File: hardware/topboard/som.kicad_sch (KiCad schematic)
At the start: 8 parts

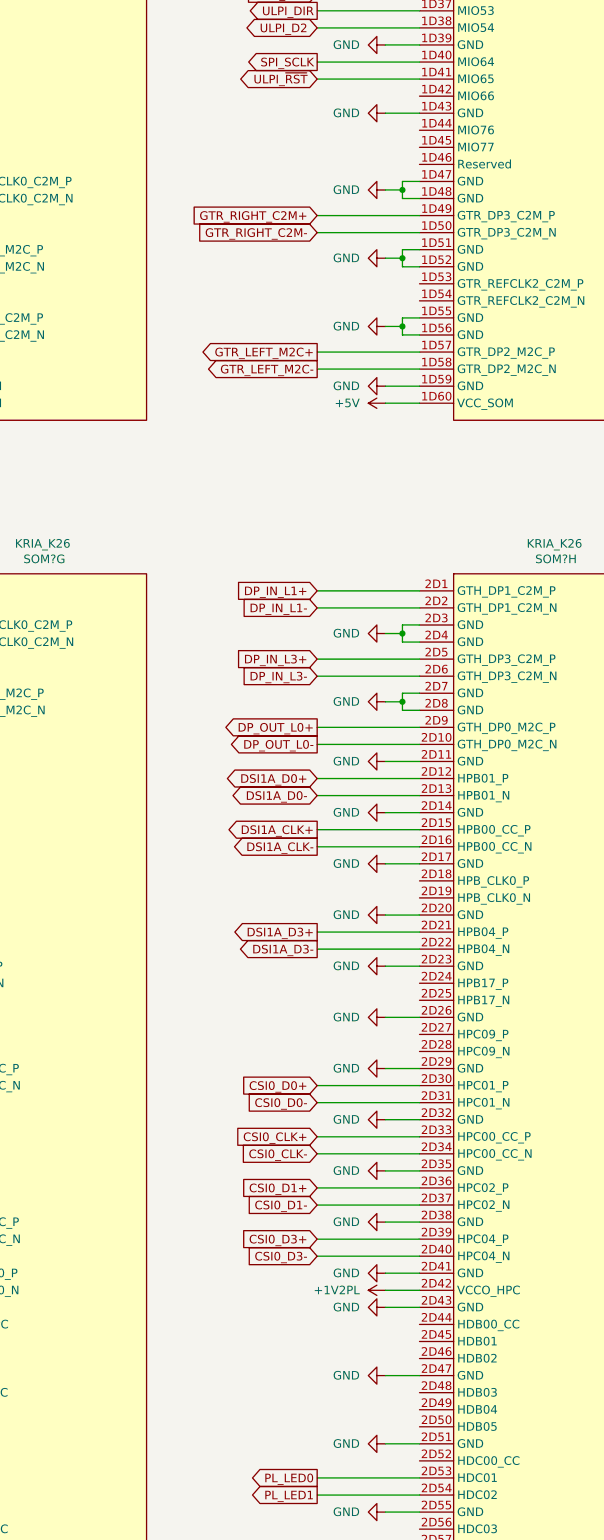
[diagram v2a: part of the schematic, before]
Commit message: Add PCIe and camera to front board
Signed-off-by: gatecat <gatecat@ds0.me>
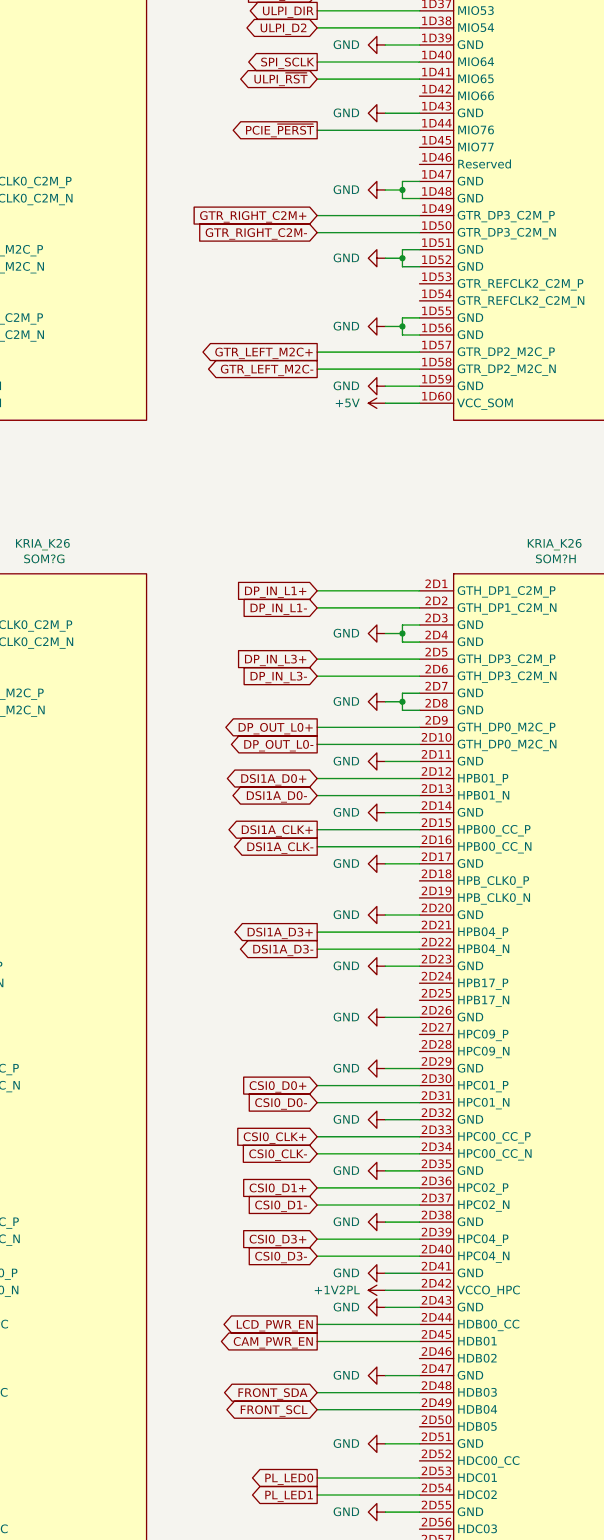
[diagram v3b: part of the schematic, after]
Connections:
- net PCIE_~{PERST}: now reaches SOM?.1D44 (MIO76)
- net LCD_PWR_EN: now reaches SOM?.2D44 (HDB00_CC)
- net CAM_PWR_EN: now reaches SOM?.2D45 (HDB01)
- net FRONT_SDA: now reaches SOM?.2D48 (HDB03)
- net FRONT_SCL: now reaches SOM?.2D49 (HDB04)
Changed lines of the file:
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@@
+    (stroke (width 0) (type default) (color 0 0 0 0))
+  )
+  (wire (pts (xy 330.2 137.16) (xy 345.44 137.16))
     (stroke (width 0) (type default) (color 0 0 0 0))
   )
@@
     (stroke (width 0) (type default) (color 0 0 0 0))
   )
+  (wire (pts (xy 330.2 314.96) (xy 345.44 314.96))
+    (stroke (width 0) (type default) (color 0 0 0 0))
+  )
+  (wire (pts (xy 330.2 317.5) (xy 345.44 317.5))
+    (stroke (width 0) (type default) (color 0 0 0 0))
+  )
+  (wire (pts (xy 330.2 325.12) (xy 345.44 325.12))
+    (stroke (width 0) (type default) (color 0 0 0 0))
+  )
+  (wire (pts (xy 330.2 327.66) (xy 345.44 327.66))
+    (stroke (width 0) (type default) (color 0 0 0 0))
+  )
   (wire (pts (xy 330.2 337.82) (xy 345.44 337.82))
     (stroke (width 0) (type default) (color 0 0 0 0))
@@
     )
   )
+  (global_label "PCIE_~{PERST}" (shape output) (at 330.2 137.16 180) (fields_autoplaced)
+    (effects (font (size 1.27 1.27)) (justify right))
+    (property "Intersheet References" "${INTERSHEET_REFS}" (id 0) (at 316.6593 137.0806 0)
+      (effects (font (size 1.27 1.27)) (justify right) hide)
+    )
+  )
   (global_label "GTR_RIGHT_C2M+" (shape input) (at 330.2 149.86 180) (fields_autoplaced)
     (effects (font (size 1.27 1.27)) (justify right))
@@
       (effects (font (size 1.27 1.27)) (justify right) hide)
     )
+  )
+  (global_label "LCD_PWR_EN" (shape output) (at 330.2 314.96 180) (fields_autoplaced)
+    (effects (font (size 1.27 1.27)) (justify right))
+    (property "Intersheet References" "${INTERSHEET_REFS}" (id 0) (at 315.8126 314.8806 0)
+      (effects (font (size 1.27 1.27)) (justify right) hide)
+    )
+  )
+  (global_label "CAM_PWR_EN" (shape output) (at 330.2 317.5 180) (fields_autoplaced)
+    (effects (font (size 1.27 1.27)) (justify right))
+    (property "Intersheet References" "${INTERSHEET_REFS}" (id 0) (at 315.5707 317.4206 0)
+      (effects (font (size 1.27 1.27)) (justify right) hide)
+    )
+  )
+  (global_label "FRONT_SDA" (shape bidirectional) (at 330.2 325.12 180) (fields_autoplaced)
+    (effects (font (size 1.27 1.27)) (justify right))
+    (property "Intersheet References" "${INTERSHEET_REFS}" (id 0) (at 317.264 325.0406 0)
+      (effects (font (size 1.27 1.27)) (justify right) hide)
+    )
+  )
+  (global_label "FRONT_SCL" (shape bidirectional) (at 330.2 327.66 180) (fields_autoplaced)
+    (effects (font (size 1.27 1.27)) (justify right))
+    (property "Intersheet References" "${INTERSHEET_REFS}" (id 0) (at 317.3245 327.5806 0)
+      (effects (font (size 1.27 1.27)) (justify right) hide)
+    )

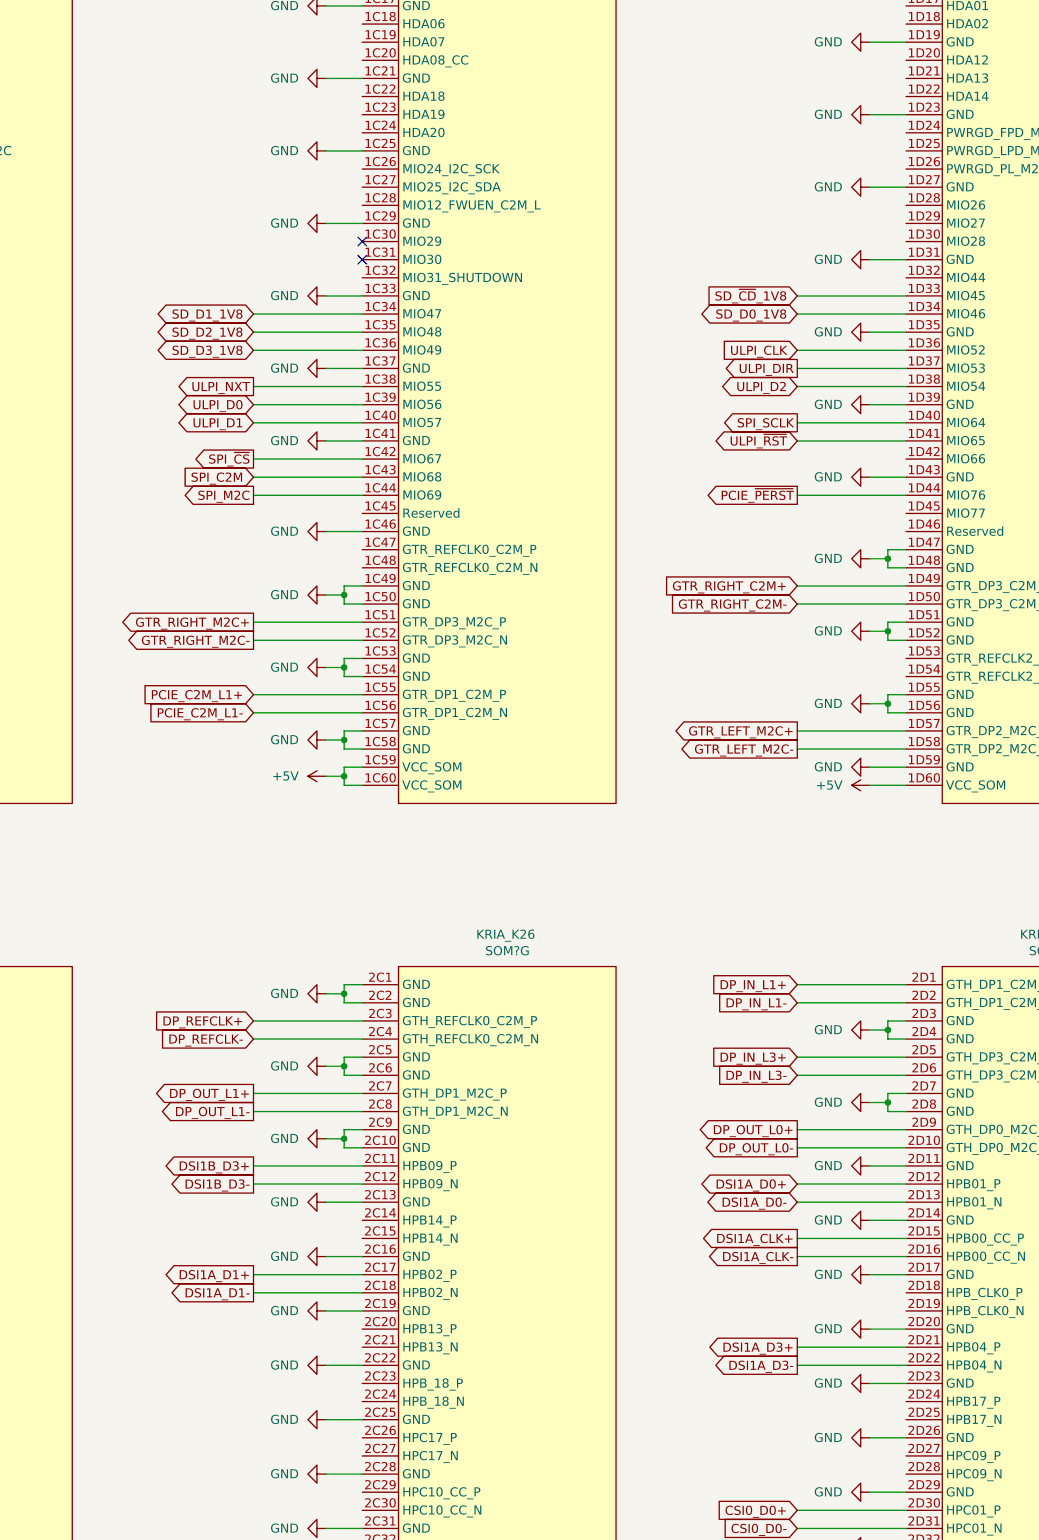
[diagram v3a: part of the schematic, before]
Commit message: Add some general control IO
Signed-off-by: gatecat <gatecat@ds0.me>
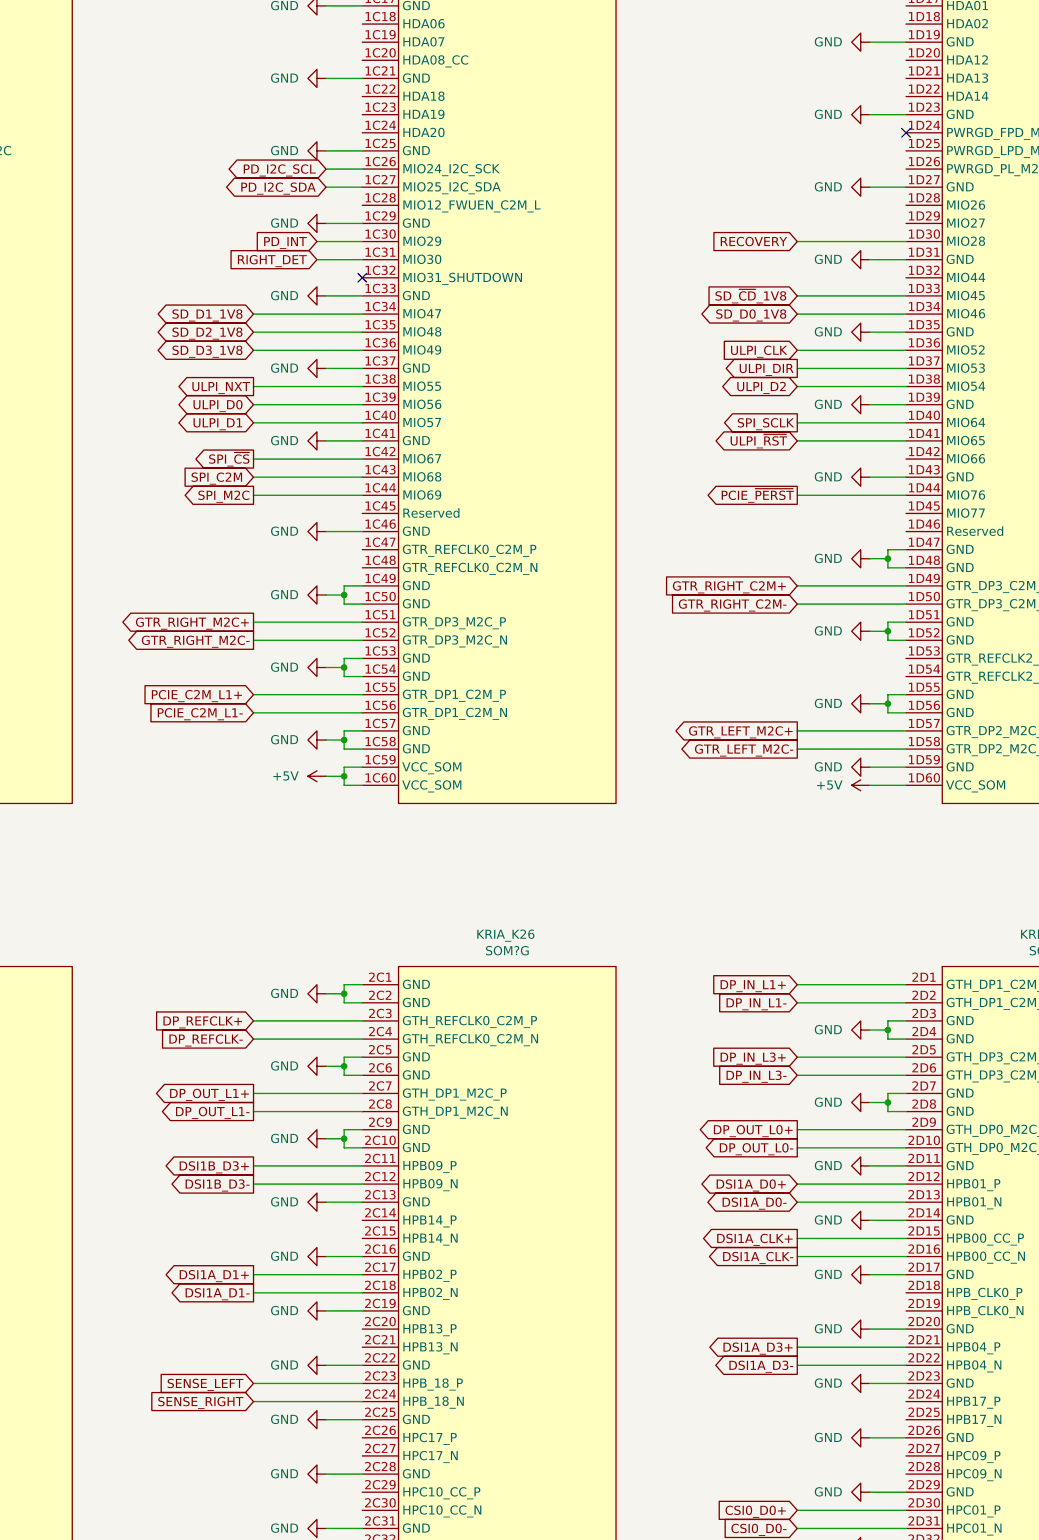
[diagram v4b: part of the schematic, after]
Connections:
- net PD_I2C_SCL: now reaches SOM?.1C26 (MIO24_I2C_SCK)
- net PD_I2C_SDA: now reaches SOM?.1C27 (MIO25_I2C_SDA)
- net PD_INT: now reaches SOM?.1C30 (MIO29)
- net RIGHT_DET: now reaches SOM?.1C31 (MIO30)
- net RECOVERY: now reaches SOM?.1D30 (MIO28)
- net SENSE_LEFT: now reaches SOM?.2C23 (HPB_18_P)
- net SENSE_RIGHT: now reaches SOM?.2C24 (HPB_18_N)
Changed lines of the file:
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@@
   (junction (at 342.9 354.33) (diameter 0) (color 0 0 0 0))
   (no_connect (at 193.04 142.24))
-  (no_connect (at 269.24 101.6))
-  (no_connect (at 269.24 104.14))
+  (no_connect (at 269.24 106.68))
+  (no_connect (at 345.44 86.36))
   (wire (pts (xy 101.6 81.28) (xy 116.84 81.28))
     (stroke (width 0) (type default) (color 0 0 0 0))
@@
     (stroke (width 0) (type default) (color 0 0 0 0))
   )
+  (wire (pts (xy 254 261.62) (xy 269.24 261.62))
+    (stroke (width 0) (type default) (color 0 0 0 0))
+  )
+  (wire (pts (xy 254 264.16) (xy 269.24 264.16))
+    (stroke (width 0) (type default) (color 0 0 0 0))
+  )
+  (wire (pts (xy 262.89 101.6) (xy 269.24 101.6))
+    (stroke (width 0) (type default) (color 0 0 0 0))
+  )
+  (wire (pts (xy 262.89 104.14) (xy 269.24 104.14))
+    (stroke (width 0) (type default) (color 0 0 0 0))
+  )
   (wire (pts (xy 264.16 29.21) (xy 266.7 29.21))
     (stroke (width 0) (type default) (color 0 0 0 0))
@@
     (stroke (width 0) (type default) (color 0 0 0 0))
   )
+  (wire (pts (xy 264.16 91.44) (xy 269.24 91.44))
+    (stroke (width 0) (type default) (color 0 0 0 0))
+  )
+  (wire (pts (xy 264.16 93.98) (xy 269.24 93.98))
+    (stroke (width 0) (type default) (color 0 0 0 0))
+  )
   (wire (pts (xy 264.16 99.06) (xy 269.24 99.06))
     (stroke (width 0) (type default) (color 0 0 0 0))
@@
     (stroke (width 0) (type default) (color 0 0 0 0))
   )
+  (wire (pts (xy 330.2 101.6) (xy 345.44 101.6))
+    (stroke (width 0) (type default) (color 0 0 0 0))
+  )
   (wire (pts (xy 330.2 109.22) (xy 345.44 109.22))
     (stroke (width 0) (type default) (color 0 0 0 0))
@@
     )
   )
+  (global_label "SENSE_LEFT" (shape input) (at 254 261.62 180) (fields_autoplaced)
+    (effects (font (size 1.27 1.27)) (justify right))
+    (property "Intersheet References" "${INTERSHEET_REFS}" (id 0) (at 240.3383 261.6994 0)
+      (effects (font (size 1.27 1.27)) (justify right) hide)
+    )
+  )
+  (global_label "SENSE_RIGHT" (shape input) (at 254 264.16 180) (fields_autoplaced)
+    (effects (font (size 1.27 1.27)) (justify right))
+    (property "Intersheet References" "${INTERSHEET_REFS}" (id 0) (at 239.1288 264.2394 0)
+      (effects (font (size 1.27 1.27)) (justify right) hide)
+    )
+  )
+  (global_label "PD_INT" (shape input) (at 262.89 101.6 180) (fields_autoplaced)
+    (effects (font (size 1.27 1.27)) (justify right))
+    (property "Intersheet References" "${INTERSHEET_REFS}" (id 0) (at 254.0664 101.5206 0)
+      (effects (font (size 1.27 1.27)) (justify right) hide)
+    )
+  )
+  (global_label "RIGHT_DET" (shape input) (at 262.89 104.14 180) (fields_autoplaced)
+    (effects (font (size 1.27 1.27)) (justify right))
+    (property "Intersheet References" "${INTERSHEET_REFS}" (id 0) (at 250.6798 104.0606 0)
+      (effects (font (size 1.27 1.27)) (justify right) hide)
+    )
+  )
   (global_label "DSI0A_CLK+" (shape output) (at 264.16 33.02 180) (fields_autoplaced)
     (effects (font (size 1.27 1.27)) (justify right))
@@
       (effects (font (size 1.27 1.27)) (justify right) hide)
     )
+  )
+  (global_label "PD_I2C_SCL" (shape bidirectional) (at 264.16 91.44 180) (fields_autoplaced)
+    (effects (font (size 1.27 1.27)) (justify right))
+    (property "Intersheet References" "${INTERSHEET_REFS}" (id 0) (at 250.6798 91.3606 0)
+      (effects (font (size 1.27 1.27)) (justify right) hide)
+    )
+  )
+  (global_label "PD_I2C_SDA" (shape bidirectional) (at 264.16 93.98 180) (fields_autoplaced)
+    (effects (font (size 1.27 1.27)) (justify right))
+    (property "Intersheet References" "${INTERSHEET_REFS}" (id 0) (at 250.6193 93.9006 0)
+      (effects (font (size 1.27 1.27)) (justify right) hide)
+    )
+  )
+  (global_label "RECOVERY" (shape input) (at 330.2 101.6 180) (fields_autoplaced)
+    (effects (font (size 1.27 1.27)) (justify right))
+    (property "Intersheet References" "${INTERSHEET_REFS}" (id 0) (at 318.1712 101.5206 0)
+      (effects (font (size 1.27 1.27)) (justify right) hide)
+    )
